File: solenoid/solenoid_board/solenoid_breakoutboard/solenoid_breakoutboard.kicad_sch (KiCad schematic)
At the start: 8 parts, among them Q1 AO4842, U1 PCA9536DP

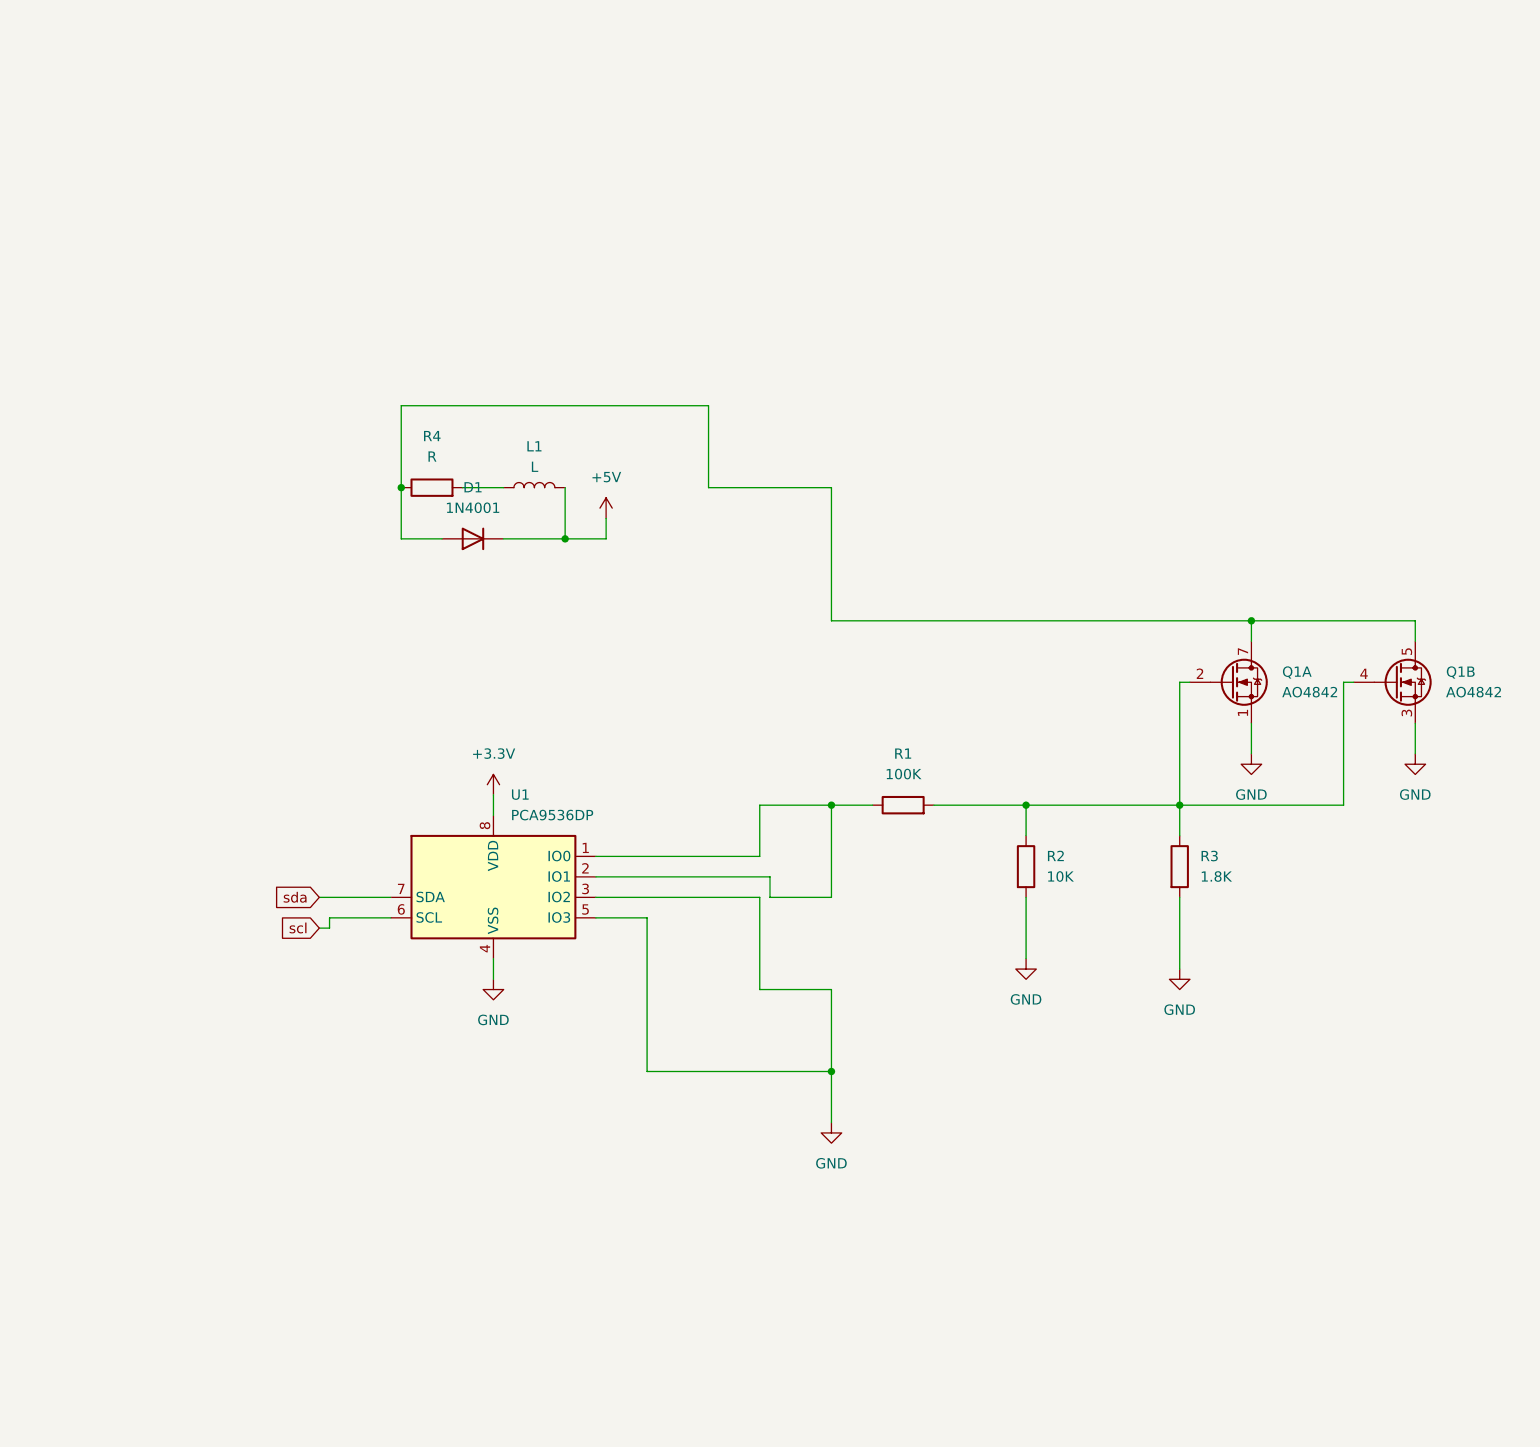
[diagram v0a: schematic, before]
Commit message: finished solenoid breakout schematic + started on PCB
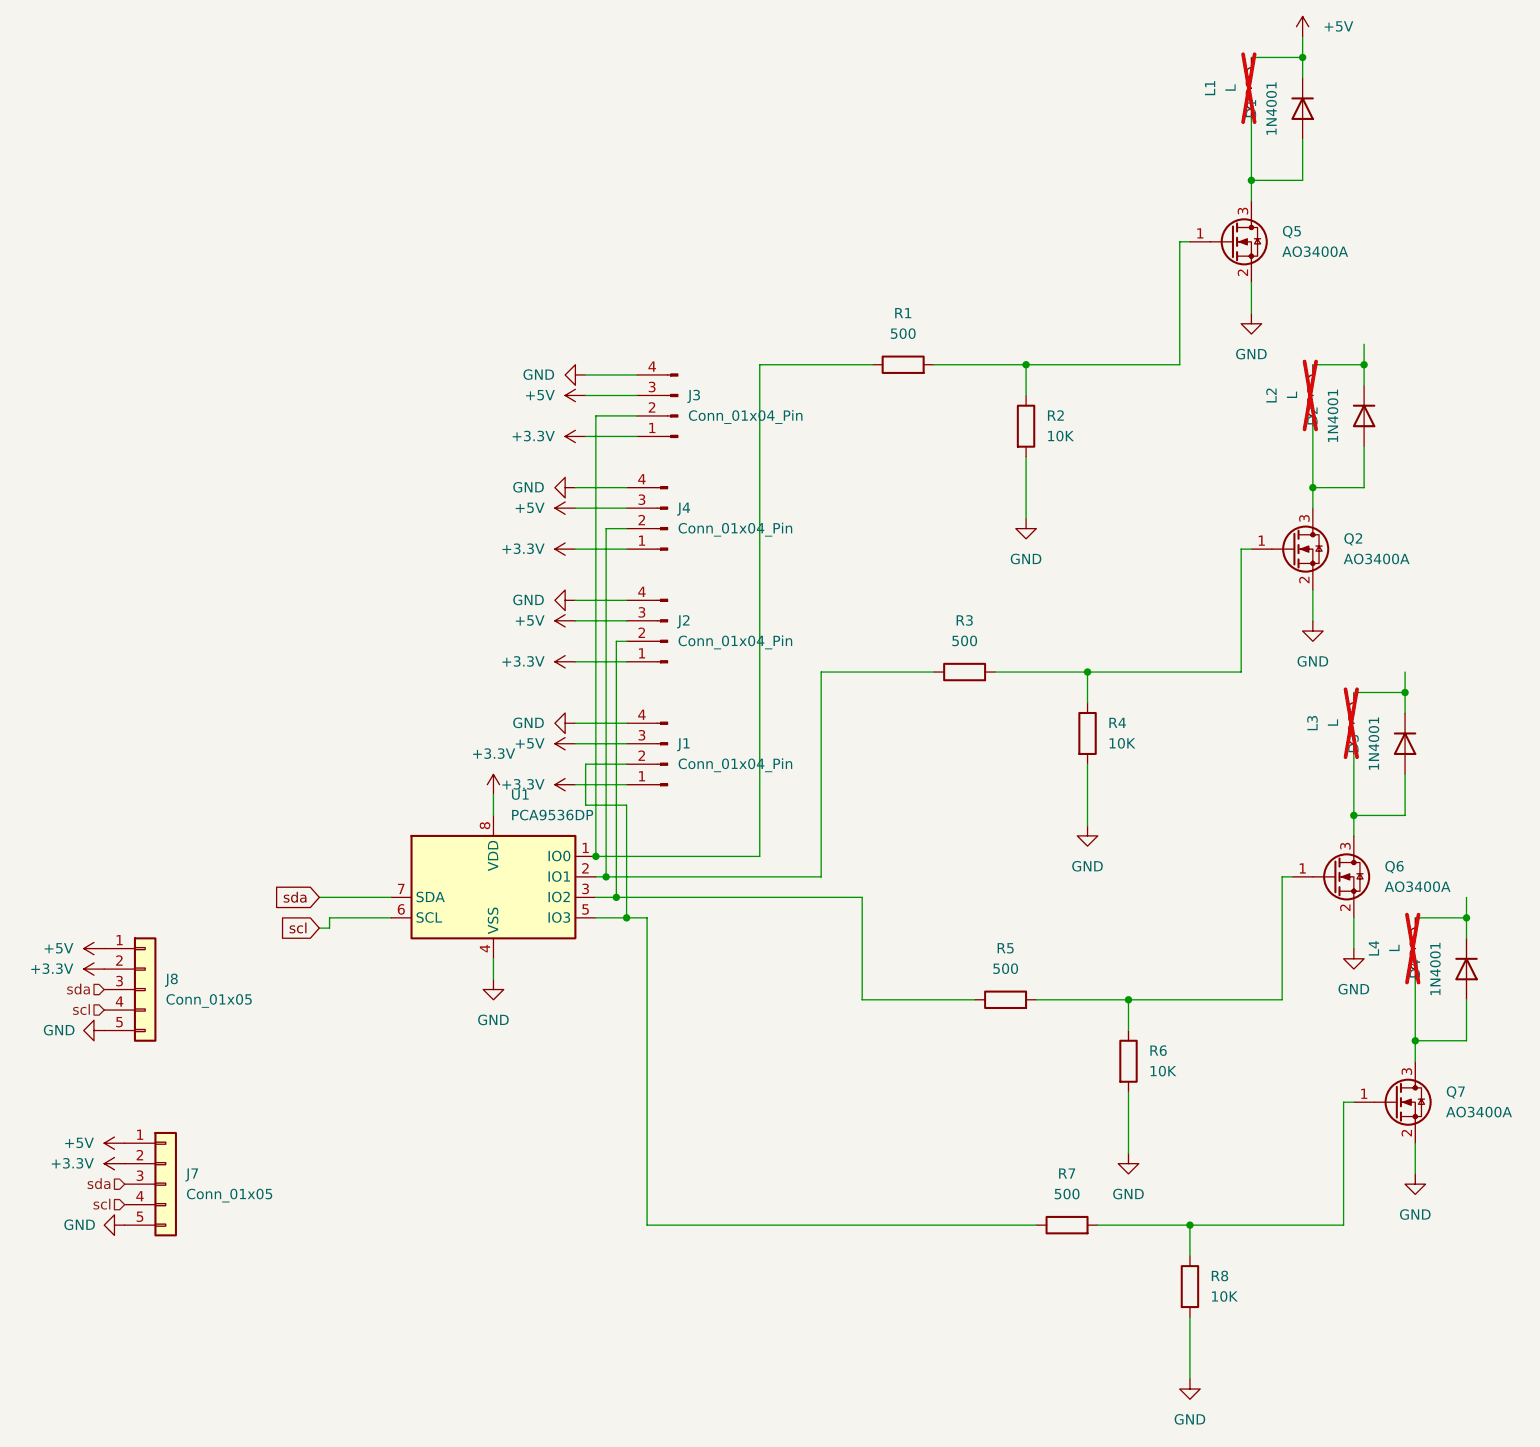
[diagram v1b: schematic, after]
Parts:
- removed Q1: AO4842, Package_SO:SOIC-8_3.9x4.9mm_P1.27mm, symbol Transistor_FET:AO4842
- added D2, D3, D4: 1N4001, Diode_SMD:D_SOD-123F, symbol Diode:1N4001
- added J1, J2, J3, J4: Conn_01x04_Pin, Connector_PinHeader_2.54mm:PinHeader_1x04_P2.54mm_Vertical, symbol Connector:Conn_01x04_Pin
- added J7, J8: Conn_01x05, Connector_PinHeader_2.54mm:PinHeader_1x05_P2.54mm_Vertical, symbol Connector_Generic:Conn_01x05
- added L2, L3, L4: L, Connector_PinHeader_2.54mm:PinHeader_1x02_P2.54mm_Vertical, symbol Device:L
- added Q2, Q5, Q6, Q7: AO3400A, Package_TO_SOT_SMD:SOT-23, symbol Transistor_FET:AO3400A
- added R5, R7: 500, Resistor_SMD:R_0603_1608Metric_Pad0.98x0.95mm_HandSolder, symbol Device:R
- added R6, R8: 10K, Resistor_SMD:R_0603_1608Metric_Pad0.98x0.95mm_HandSolder, symbol Device:R
- D1: footprint Diode_THT:D_DO-41_SOD81_P10.16mm_Horizontal -> Diode_SMD:D_SOD-123F
- L1: footprint Inductor_THT:L_Radial_D10.0mm_P5.00mm_Fastron_07M -> Connector_PinHeader_2.54mm:PinHeader_1x02_P2.54mm_Vertical; now not fitted
- R1: value 100K -> 500; footprint Resistor_SMD:R_0805_2012Metric -> Resistor_SMD:R_0603_1608Metric_Pad0.98x0.95mm_HandSolder
- R2: footprint Resistor_SMD:R_0805_2012Metric -> Resistor_SMD:R_0603_1608Metric_Pad0.98x0.95mm_HandSolder
- R3: value 1.8K -> 500; footprint Resistor_SMD:R_0805_2012Metric -> Resistor_SMD:R_0603_1608Metric_Pad0.98x0.95mm_HandSolder
- R4: value R -> 10K; footprint Resistor_SMD:R_0805_2012Metric -> Resistor_SMD:R_0603_1608Metric_Pad0.98x0.95mm_HandSolder
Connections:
- net +3.3V: now also J1.1 (Pin_1), J2.1 (Pin_1), J3.1 (Pin_1), J4.1 (Pin_1), J7.2 (Pin_2), J8.2 (Pin_2)
- net +5V: now also J1.3 (Pin_3), J2.3 (Pin_3), J3.3 (Pin_3), J4.3 (Pin_3), J7.1 (Pin_1), J8.1 (Pin_1)
- net GND: now also R4.2, J1.4 (Pin_4), J2.4 (Pin_4), J3.4 (Pin_4), J4.4 (Pin_4), J7.5 (Pin_5), J8.5 (Pin_5), Q2.2 (S), Q5.2 (S), Q6.2 (S), Q7.2 (S), R6.2, R8.2; no longer R3.2, U1.3 (IO2), U1.5 (IO3)
- net scl: now also J7.4 (Pin_4), J8.4 (Pin_4)
- net sda: now also J7.3 (Pin_3), J8.3 (Pin_3)
- net at D1.2 (A): now also L1.1, Q5.3 (D); no longer R4.1
- net at R1.2, R2.1: now also Q5.1 (G); no longer R3.1
- net at R1.1, U1.1 (IO0): now also J3.2 (Pin_2); no longer U1.2 (IO1)
- new net: J1.2 (Pin_2), R7.1, U1.5 (IO3)
- new net: Q6.1 (G), R5.2, R6.1
- new net: D3.2 (A), L3.1, Q6.3 (D)
- new net: Q7.1 (G), R7.2, R8.1
- new net: D3.1 (K), L3.2
- new net: J4.2 (Pin_2), R3.1, U1.2 (IO1)
- new net: D2.2 (A), L2.1, Q2.3 (D)
- new net: D2.1 (K), L2.2
- new net: D4.2 (A), L4.1, Q7.3 (D)
- new net: D4.1 (K), L4.2
- new net: Q2.1 (G), R3.2, R4.1
- new net: J2.2 (Pin_2), R5.1, U1.3 (IO2)
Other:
- moved on the sheet: D1, R1, R2
